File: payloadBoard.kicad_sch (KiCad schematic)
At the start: 0 parts

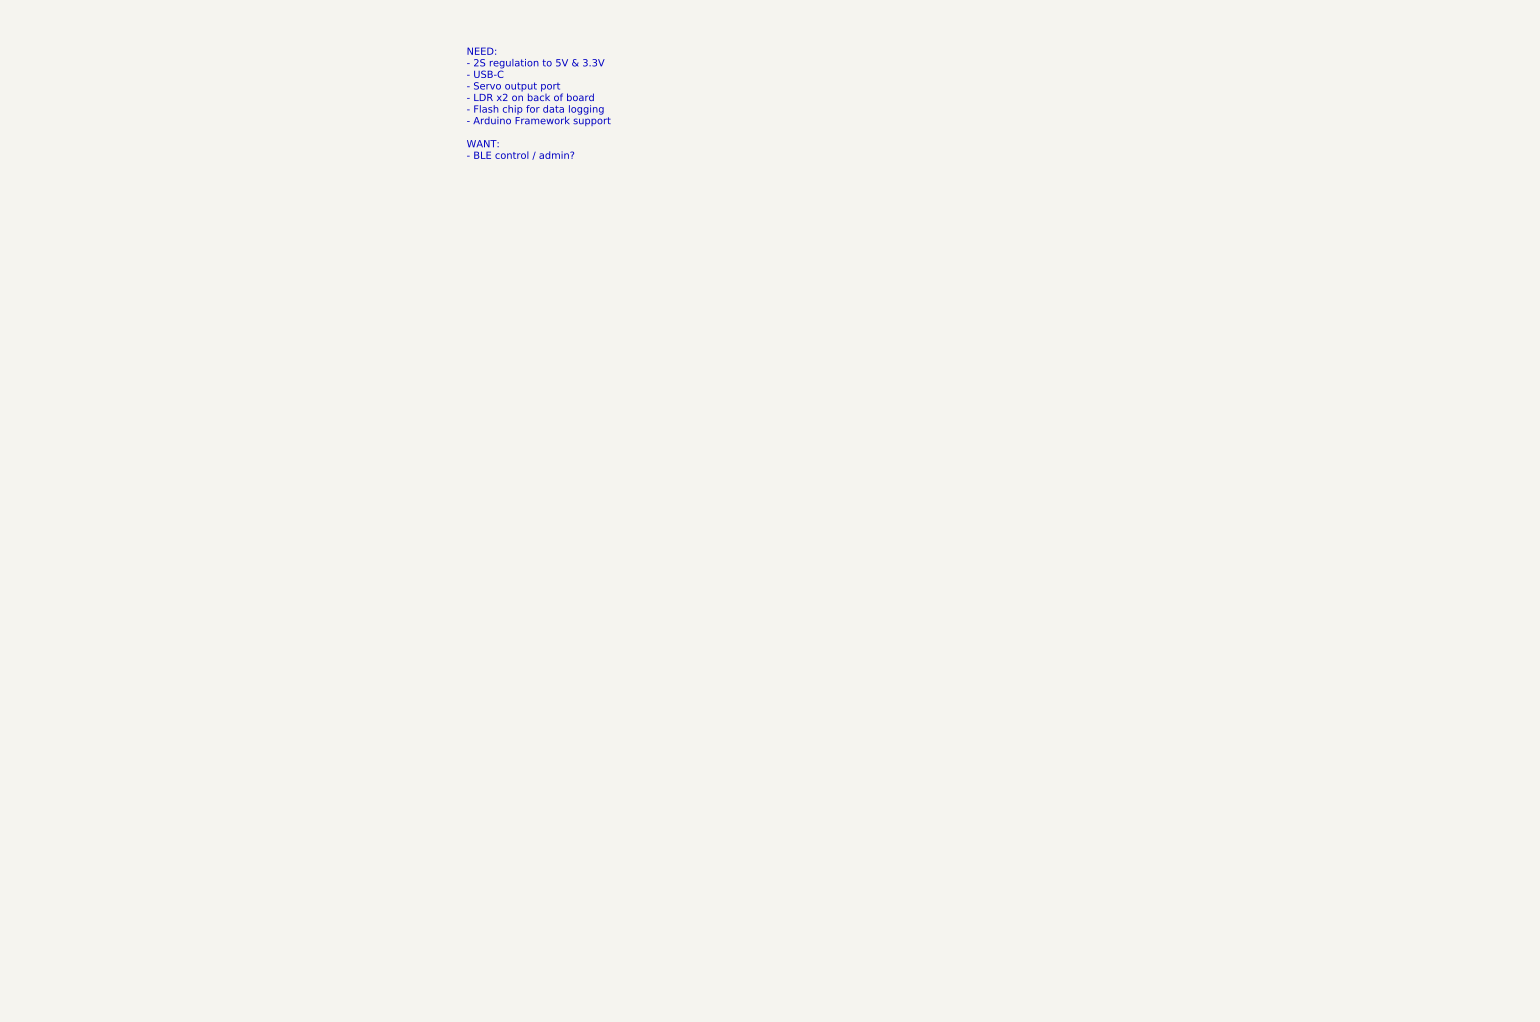
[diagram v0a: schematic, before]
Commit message: most schematic minus power
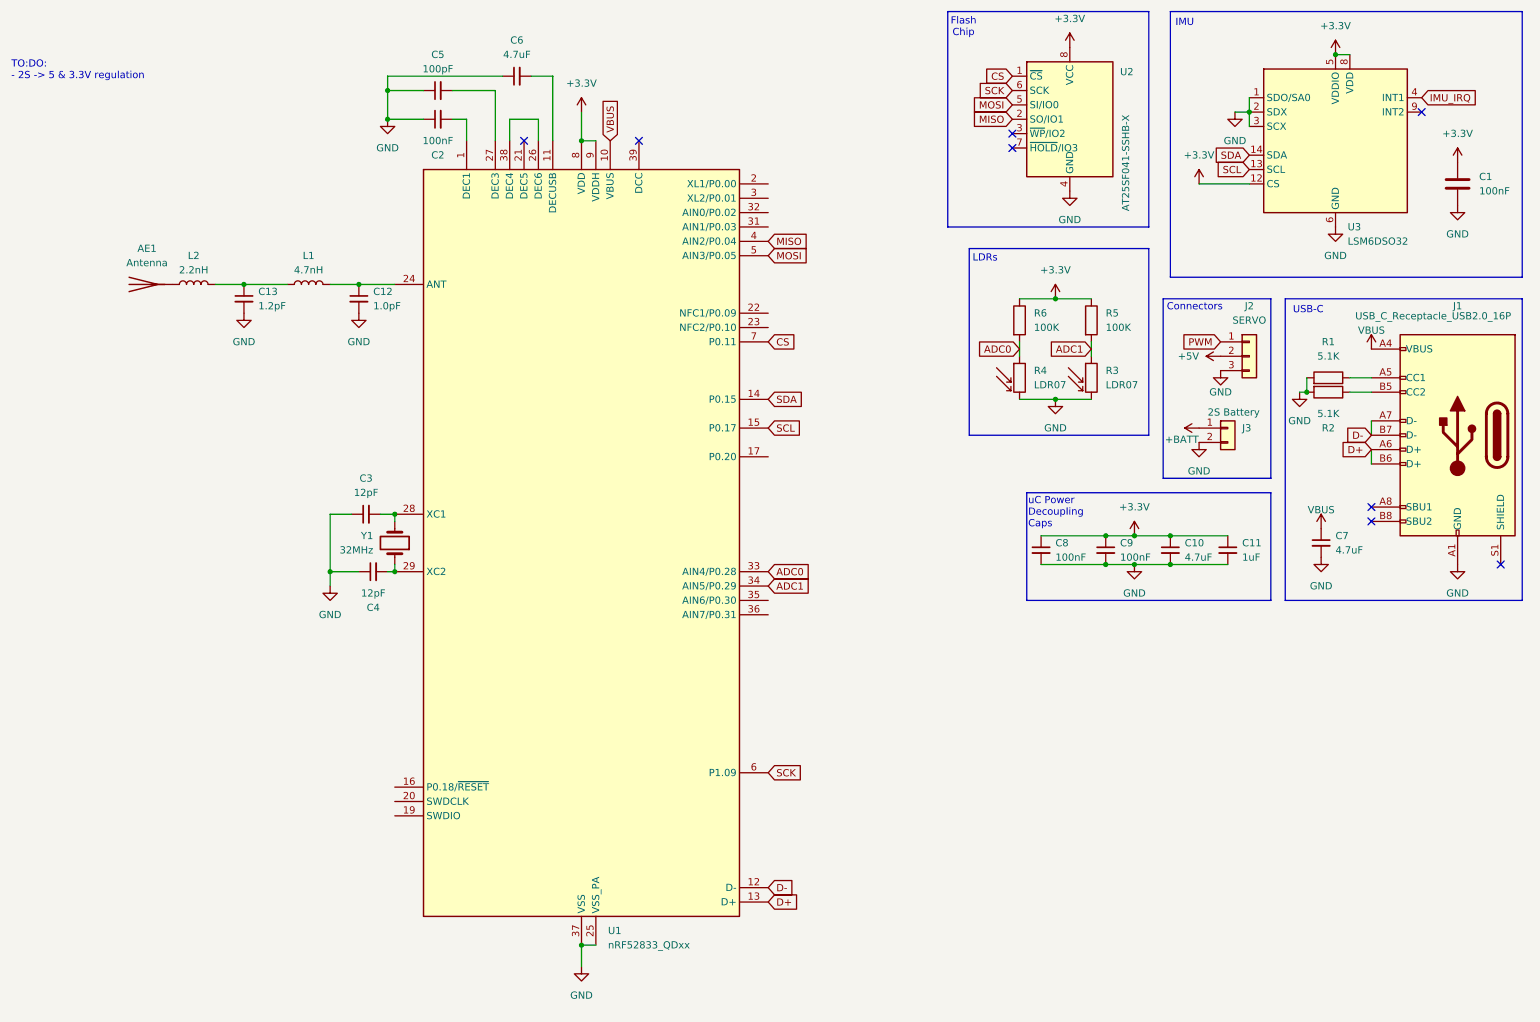
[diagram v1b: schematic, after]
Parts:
- added AE1: Antenna, symbol Device:Antenna
- added C1: 100nF, Capacitor_SMD:C_0402_1005Metric, symbol Device:C
- added C10, C6, C7: 4.7uF, Capacitor_SMD:C_0402_1005Metric, symbol Device:C_Small
- added C11: 1uF, Capacitor_SMD:C_0402_1005Metric, symbol Device:C_Small
- added C12: 1.0pF, Capacitor_SMD:C_0402_1005Metric, symbol Device:C_Small
- added C13: 1.2pF, Capacitor_SMD:C_0402_1005Metric, symbol Device:C_Small
- added C2, C8, C9: 100nF, Capacitor_SMD:C_0402_1005Metric, symbol Device:C_Small
- added C3, C4: 12pF, Capacitor_SMD:C_0402_1005Metric, symbol Device:C_Small
- added C5: 100pF, Capacitor_SMD:C_0402_1005Metric, symbol Device:C_Small
- added J1: USB_C_Receptacle_USB2.0_16P, Connector_USB:USB_C_Receptacle_GCT_USB4105-xx-A_16P_TopMnt_Horizontal, symbol Connector:USB_C_Receptacle_USB2.0_16P
- added J2: SERVO, Connector_PinHeader_2.54mm:PinHeader_1x03_P2.54mm_Vertical, symbol Connector_Generic:Conn_01x03
- added J3: 2S Battery, Connector_PinHeader_2.54mm:PinHeader_1x02_P2.54mm_Vertical, symbol Connector_Generic:Conn_01x02
- added L1: 4.7nH, Capacitor_SMD:C_0402_1005Metric, symbol Device:L
- added L2: 2.2nH, Capacitor_SMD:C_0402_1005Metric, symbol Device:L
- added R1, R2: 5.1K, Resistor_SMD:R_0402_1005Metric, symbol Device:R
- added R3, R4: LDR07, OptoDevice:R_LDR_5.1x4.3mm_P3.4mm_Vertical, symbol Sensor_Optical:LDR07
- added R5, R6: 100K, Resistor_SMD:R_0402_1005Metric, symbol Device:R
- added U1: nRF52833_QDxx, Package_DFN_QFN:QFN-40-1EP_5x5mm_P0.4mm_EP3.6x3.6mm, symbol MCU_Nordic:nRF52833_QDxx
- added U2: AT25SF041-SSHB-X, Package_SO:SOIC-8_3.9x4.9mm_P1.27mm, symbol Memory_Flash:AT25SF081-SSHD-X
- added U3: LSM6DSO32, Package_LGA:LGA-14_3x2.5mm_P0.5mm_LayoutBorder3x4y, symbol Sensor_Motion:LSM6DS3
- added Y1: 32MHz, symbol Device:Crystal
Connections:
- new net: C3.2, U1.28 (XC1), Y1.2
- new net: J1.B5 (CC2), R2.1
- new net: C13.1, L1.1, L2.2
- new net: C6.2, U1.11 (DECUSB)
- new net: C4.2, U1.29 (XC2), Y1.1
- new net: C12.1, L1.2, U1.24 (ANT)
- new net: AE1.1 (A), L2.1
- new net: J1.A5 (CC1), R1.1
- new net: C2.2, U1.1 (DEC1)
- new net: U1.26 (DEC6), U1.38 (DEC4)
- new net: C5.2, U1.27 (DEC3)
- new net +3.3V: C1.1, C10.1, C11.1, C8.1, C9.1, R5.1, R6.1, U1.18 (VDD), U1.30 (VDD), U1.40 (VDD), U1.8 (VDD), U1.9 (VDDH), U2.8 (VCC), U3.12 (CS), U3.5 (VDDIO), U3.8 (VDD)
- new net +5V: J2.2 (Pin_2)
- new net +BATT: J3.1 (Pin_1)
- new net ADC0: R4.1, R6.2, U1.33 (AIN4/P0.28)
- new net ADC1: R3.1, R5.2, U1.34 (AIN5/P0.29)
- new net CS: U1.7 (P0.11), U2.1 (~{CS})
- new net D+: J1.A6 (D+), J1.B6 (D+), U1.13 (D+)
- new net D-: J1.A7 (D-), J1.B7 (D-), U1.12 (D-)
- new net GND: C1.2, C10.2, C11.2, C12.2, C13.2, C2.1, C3.1, C4.1, C5.1, C6.1, C7.2, C8.2, C9.2, J1.A1 (GND), J1.A12 (GND), J1.B1 (GND), J1.B12 (GND), J2.3 (Pin_3), J3.2 (Pin_2), R1.2, R2.2, R3.2, R4.2, U1.25 (VSS_PA), U1.37 (VSS), U1.41 (VSS), U2.4 (GND), U3.1 (SDO/SA0), U3.2 (SDX), U3.3 (SCX), U3.6 (GND), U3.7 (GND)
- new net IMU_IRQ: U3.4 (INT1)
- new net MISO: U1.4 (AIN2/P0.04), U2.2 (SO/IO1)
- new net MOSI: U1.5 (AIN3/P0.05), U2.5 (SI/IO0)
- new net PWM: J2.1 (Pin_1)
- new net SCK: U1.6 (P1.09), U2.6 (SCK)
- new net SCL: U1.15 (P0.17), U3.13 (SCL)
- new net SDA: U1.14 (P0.15), U3.14 (SDA)
- new net VBUS: C7.1, J1.A4 (VBUS), J1.A9 (VBUS), J1.B4 (VBUS), J1.B9 (VBUS), U1.10 (VBUS)
- no-connect marks 0 -> 8
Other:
- note added: "Connectors"
- note added: "Flash Chip"
- note added: "IMU"
- note added: "LDRs"
- note added: "TO:DO: - 2S -> 5 & 3.3V regulation"
- note added: "USB-C"
- note added: "uC Power Decoupling Caps"
- note removed: "NEED: - 2S regulation to 5V & 3.3V - USB-C - Servo output port - LDR x2 on back of board - Flash chip for data logging - Arduino Framework support WANT: - BLE control / admin?"

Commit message: all footprints in but antenna, review w. sophia done
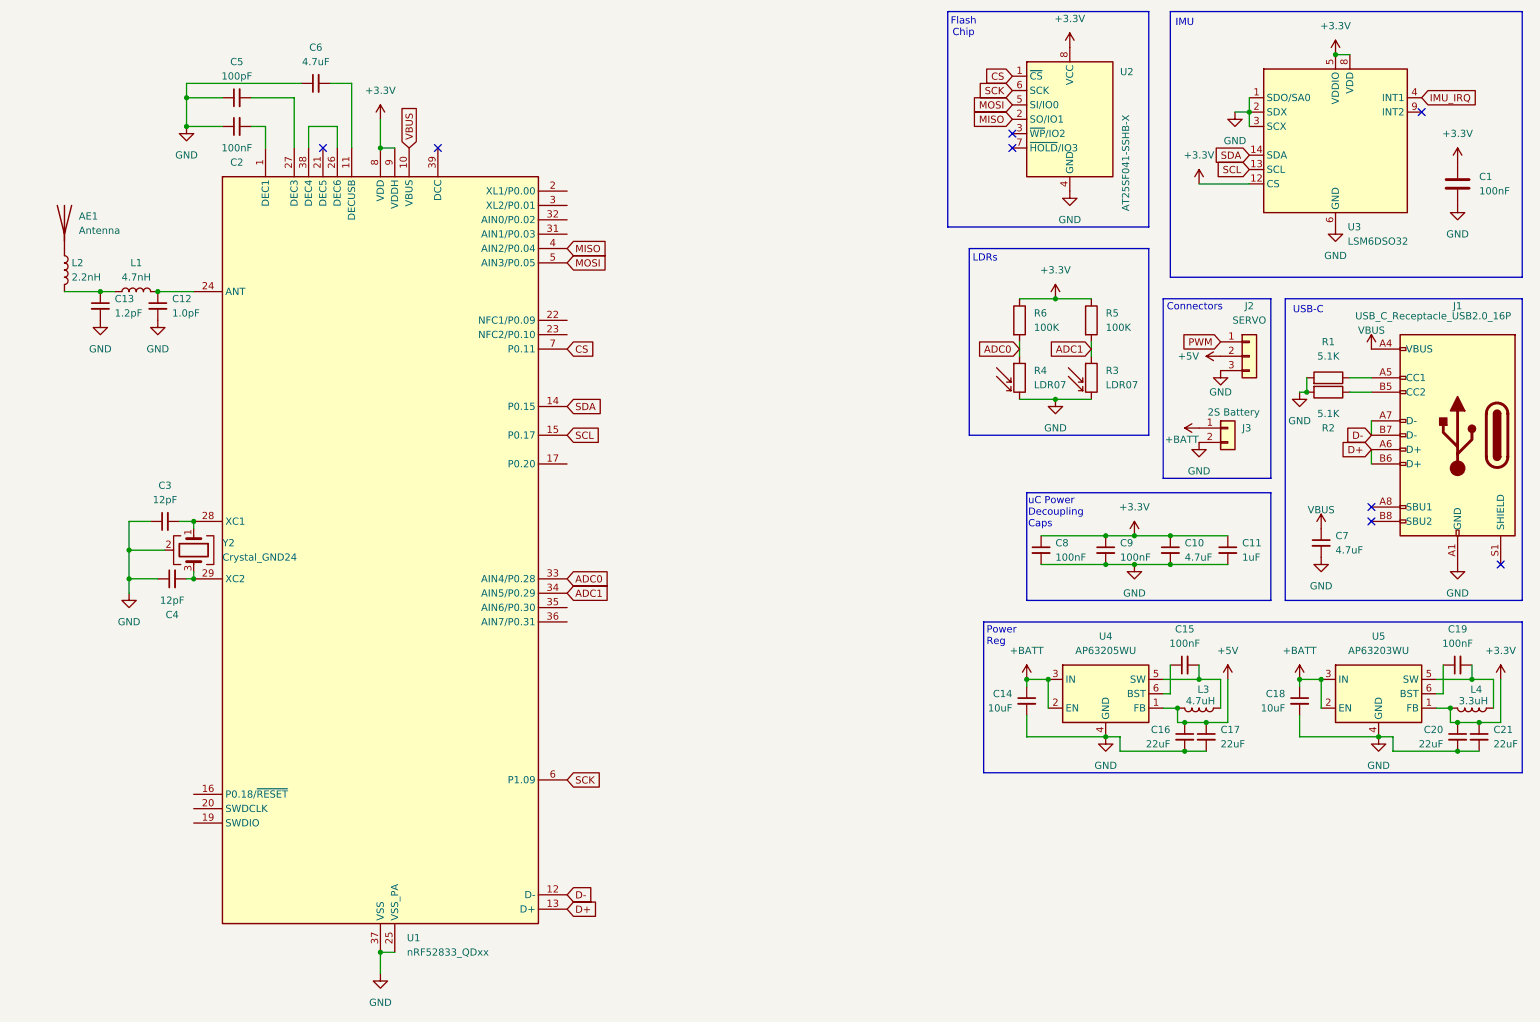
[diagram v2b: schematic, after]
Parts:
- removed Y1: 32MHz, symbol Device:Crystal
- added C14, C18: 10uF, Capacitor_SMD:C_0603_1608Metric, symbol Device:C_Small
- added C15, C19: 100nF, Capacitor_SMD:C_0402_1005Metric, symbol Device:C_Small
- added C16, C17, C20, C21: 22uF, Capacitor_SMD:C_0603_1608Metric, symbol Device:C_Small
- added L3: 4.7uH, Inductor_SMD:L_1008_2520Metric, symbol Device:L
- added L4: 3.3uH, Inductor_SMD:L_1008_2520Metric, symbol Device:L
- added U4: AP63205WU, Package_TO_SOT_SMD:TSOT-23-6, symbol Regulator_Switching:AP63205WU
- added U5: AP63203WU, Package_TO_SOT_SMD:TSOT-23-6, symbol Regulator_Switching:AP63203WU
- added Y2: Crystal_GND24, Crystal:Crystal_SMD_3225-4Pin_3.2x2.5mm, symbol Device:Crystal_GND24
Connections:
- net +3.3V: now also C20.1, C21.1, L4.2, U5.1 (FB)
- net +5V: now also C16.1, C17.1, L3.2, U4.1 (FB)
- net +BATT: now also C14.1, C18.1, U4.2 (EN), U4.3 (IN), U5.2 (EN), U5.3 (IN)
- net GND: now also C14.2, C16.2, C17.2, C18.2, C20.2, C21.2, U4.4 (GND), U5.4 (GND), Y2.2 (G), Y2.4 (G)
- net at C3.2, U1.28 (XC1): now also Y2.1
- net at C4.2, U1.29 (XC2): now also Y2.3
- new net: C15.1, U4.6 (BST)
- new net: C15.2, L3.1, U4.5 (SW)
- new net: C19.2, L4.1, U5.5 (SW)
- new net: C19.1, U5.6 (BST)
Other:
- note added: "Power Reg"
- note removed: "TO:DO: - 2S -> 5 & 3.3V regulation"
- moved on the sheet: AE1, C12, C13, C2, C3, C4, C5, C6, L1, L2, U1

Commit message: version 1 finished
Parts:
- removed AE1: Antenna, symbol Device:Antenna
- added AE1: Antenna_Chip, RF_Antenna:Texas_SWRA117D_2.4GHz_Left, symbol Device:Antenna_Chip
- added C22: 1uF, Capacitor_SMD:C_0402_1005Metric, symbol Device:C_Small
- added J4: Conn_01x04, Connector_PinSocket_1.00mm:PinSocket_1x04_P1.00mm_Vertical, symbol Connector_Generic:Conn_01x04
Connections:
- net IMU_IRQ is gone; now on net IMU_IRQ1: U3.4 (INT1)
- net +BATT: no longer U4.2 (EN)
- net GND: now also AE1.2 (PCB_Trace), C22.2, J4.4 (Pin_4)
- net PWM: now also U1.17 (P0.20)
- net at L2.1: now also AE1.1 (FEED)
- net at U1.16 (P0.18/~{RESET}): now also J4.1 (Pin_1)
- net at U1.19 (SWDIO): now also J4.2 (Pin_2)
- net at U1.20 (SWDCLK): now also J4.3 (Pin_3)
- net at U1.26 (DEC6), U1.38 (DEC4): now also C22.1
- net +5V_EN: now reaches U1.32 (AIN0/P0.02)
- net +5V_EN: now also U4.2 (EN)
- net IMU_IRQ1: now reaches U1.35 (AIN6/P0.30)
- no-connect marks 8 -> 14
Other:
- moved on the sheet: C6

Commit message: done other than funny silkscreen
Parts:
- added D1, D2: LED, LED_SMD:LED_0603_1608Metric, symbol Device:LED
- added R7, R8: 200, Resistor_SMD:R_0402_1005Metric, symbol Device:R_Small
- added TP1, TP2: TestPoint, Antenna:0.75x0.75_TestPad, symbol Connector:TestPoint
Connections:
- net +3.3V: now also D1.2 (A)
- net GND: now also R7.2, R8.2
- net SCL: now also TP1.1
- net SDA: now also TP2.1
- net LED: now reaches U1.2 (XL1/P0.00)
- net LED: now also D2.2 (A)
- new net: D1.1 (K), R7.1
- new net: D2.1 (K), R8.1
- no-connect marks 14 -> 13
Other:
- note added: "LEDs"
